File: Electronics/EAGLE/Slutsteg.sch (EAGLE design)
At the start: 152 parts, among them CN1 OSTYK33102030-2, CN2 OSTYK33102030-2, CN3 OSTYK33102030-2, IC1 SPX1117M3-L-3-3_TR, IC10 LM324D, IC11 L78M12ABDT-TR, IC3 ESP32-WROVER-IE-4MB, IC4 TM8211, IC6 TPA3244DDWR, IC7 TPA3251D2DDVR, IC8 LM324D, IC9 LM324D, J1 0532610671, J2 JW-PJ-307-4H, J3 B2P-VH_LF__SN_, SW3 PDB181-K420F-103A2

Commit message: started on the smaller components
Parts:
- added IC2: L78M12ABDT-TR, SamacSys_Parts:L78M12ABDT-TR
- added SJ1: (no value), jumper:SJ
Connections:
- new net VDD2: C47.+, C52.1, IC2.OUTPUT, IC7.VDD, R23.1, R24.1, SJ1.2
- net GND: now also IC2.GND_(THERMALPAD)
- net PVDD: now also IC2.INPUT
- net VDD: now also SJ1.1; no longer C47.+, C52.1, IC7.VDD, R23.1, R24.1
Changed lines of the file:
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@@
 <part name="GND6" library="supply1" library_urn="urn:adsk.eagle:library:371" deviceset="GND" device=""/>
 <part name="GND8" library="supply1" library_urn="urn:adsk.eagle:library:371" deviceset="GND" device=""/>
-<part name="VDD1" library="supply1" library_urn="urn:adsk.eagle:library:371" deviceset="VDD" device=""/>
 <part name="R25" library="rcl" library_urn="urn:adsk.eagle:library:334" deviceset="R-EU_" device="R0603" package3d_urn="urn:adsk.eagle:package:23555/3" value="20K/5%/0.1W"/>
 <part name="FRAME4" library="frames" library_urn="urn:adsk.eagle:library:229" deviceset="A3L-LOC" device=""/>
@@
 <part name="J3" library="SamacSys_Parts" deviceset="B2P-VH_LF__SN_" device="" override_package3d_urn="urn:adsk.eagle:package:27321884/2" override_package_urn="urn:adsk.eagle:footprint:27321885/1"/>
 <part name="GND11" library="supply1" library_urn="urn:adsk.eagle:library:371" deviceset="GND" device=""/>
+<part name="IC2" library="SamacSys_Parts" deviceset="L78M12ABDT-TR" device="" override_package3d_urn="urn:adsk.eagle:package:27319245/2" override_package_urn="urn:adsk.eagle:footprint:27319266/1"/>
+<part name="GND12" library="supply1" library_urn="urn:adsk.eagle:library:371" deviceset="GND" device=""/>
+<part name="SJ1" library="jumper" library_urn="urn:adsk.eagle:library:252" deviceset="SJ" device="" package3d_urn="urn:adsk.eagle:package:15471/1"/>
+<part name="VDD1" library="supply1" library_urn="urn:adsk.eagle:library:371" deviceset="VDD" device=""/>
 </parts>
 <sheets>
@@
 <attribute name="VALUE" x="35.56" y="149.86" size="1.778" layer="96" rot="MR0"/>
 </instance>
+<instance part="IC2" gate="G$1" x="116.84" y="124.46" smashed="yes" rot="MR0">
+<attribute name="NAME" x="92.71" y="132.08" size="1.778" layer="95" align="center-left"/>
+<attribute name="VALUE" x="92.71" y="129.54" size="1.778" layer="96" align="center-left"/>
+</instance>
+<instance part="GND12" gate="1" x="68.58" y="111.76" smashed="yes" rot="MR0">
+<attribute name="VALUE" x="71.12" y="109.22" size="1.778" layer="96" rot="MR0"/>
+</instance>
+<instance part="SJ1" gate="1" x="149.86" y="121.92" smashed="yes" rot="R180">
+<attribute name="NAME" x="152.4" y="119.38" size="1.778" layer="95" rot="R180"/>
+<attribute name="VALUE" x="152.4" y="125.73" size="1.778" layer="96" rot="R180"/>
+</instance>
+<instance part="VDD1" gate="G$1" x="165.1" y="139.7" smashed="yes" rot="MR0">
+<attribute name="VALUE" x="167.64" y="142.24" size="1.778" layer="96" rot="MR180"/>
+</instance>
 </instances>
 <busses>
@@
 <wire x1="33.02" y1="190.5" x2="33.02" y2="154.94" width="0.1524" layer="91"/>
 </segment>
+<segment>
+<pinref part="IC2" gate="G$1" pin="GND_(THERMALPAD)"/>
+<pinref part="GND12" gate="1" pin="GND"/>
+<wire x1="71.12" y1="124.46" x2="68.58" y2="124.46" width="0.1524" layer="91"/>
+<wire x1="68.58" y1="124.46" x2="68.58" y2="114.3" width="0.1524" layer="91"/>
+</segment>
 </net>
 <net name="SPEAKER_L_0" class="0">
@@
 <wire x1="33.02" y1="193.04" x2="33.02" y2="228.6" width="0.1524" layer="91"/>
 <label x="33.02" y="228.6" size="1.778" layer="95" xref="yes"/>
+</segment>
+<segment>
+<pinref part="IC2" gate="G$1" pin="INPUT"/>
+<wire x1="116.84" y1="124.46" x2="121.92" y2="124.46" width="0.1524" layer="91"/>
+<wire x1="121.92" y1="124.46" x2="121.92" y2="142.24" width="0.1524" layer="91"/>
+<label x="121.92" y="142.24" size="1.778" layer="95" xref="yes"/>
 </segment>
 </net>
@@
 <wire x1="144.78" y1="175.26" x2="144.78" y2="190.5" width="0.1524" layer="91"/>
 <junction x="144.78" y="190.5"/>
+</segment>
+<segment>
+<pinref part="SJ1" gate="1" pin="1"/>
+<wire x1="154.94" y1="121.92" x2="165.1" y2="121.92" width="0.1524" layer="91"/>
+<pinref part="VDD1" gate="G$1" pin="VDD"/>
+<wire x1="165.1" y1="121.92" x2="165.1" y2="137.16" width="0.1524" layer="91"/>
 </segment>
 </net>
@@
 <wire x1="337.82" y1="160.02" x2="332.74" y2="160.02" width="0.1524" layer="91"/>
 <label x="332.74" y="160.02" size="1.778" layer="95" rot="R180" xref="yes"/>
+</segment>
+</net>
+<net name="VDD2" class="0">
+<segment>
+<pinref part="IC2" gate="G$1" pin="OUTPUT"/>
+<wire x1="116.84" y1="121.92" x2="139.7" y2="121.92" width="0.1524" layer="91"/>
+<wire x1="139.7" y1="121.92" x2="139.7" y2="129.54" width="0.1524" layer="91"/>
+<label x="139.7" y="129.54" size="1.778" layer="95" xref="yes"/>
+<pinref part="SJ1" gate="1" pin="2"/>
+<wire x1="144.78" y1="121.92" x2="139.7" y2="121.92" width="0.1524" layer="91"/>
+<junction x="139.7" y="121.92"/>
 </segment>
 </net>
@@
 <instance part="GND8" gate="1" x="127" y="162.56" smashed="yes">
 <attribute name="VALUE" x="124.46" y="160.02" size="1.778" layer="96"/>
-</instance>
-<instance part="VDD1" gate="G$1" x="99.06" y="205.74" smashed="yes">
-<attribute name="VALUE" x="99.06" y="208.28" size="1.778" layer="96"/>
 </instance>
 <instance part="R25" gate="G$1" x="139.7" y="149.86" smashed="yes">
@@
 </segment>
 </net>
-<net name="VDD" class="0">
-<segment>
-<wire x1="121.92" y1="111.76" x2="99.06" y2="111.76" width="0.1524" layer="91"/>
-<wire x1="99.06" y1="111.76" x2="99.06" y2="185.42" width="0.1524" layer="91"/>
-<wire x1="99.06" y1="185.42" x2="99.06" y2="203.2" width="0.1524" layer="91"/>
-<junction x="99.06" y="185.42"/>
-<pinref part="IC7" gate="G$1" pin="VDD"/>
-<wire x1="139.7" y1="162.56" x2="147.32" y2="162.56" width="0.1524" layer="91"/>
-<wire x1="139.7" y1="185.42" x2="139.7" y2="162.56" width="0.1524" layer="91"/>
-<pinref part="R24" gate="G$1" pin="1"/>
-<pinref part="VDD1" gate="G$1" pin="VDD"/>
-<wire x1="99.06" y1="185.42" x2="114.3" y2="185.42" width="0.1524" layer="91"/>
-<wire x1="114.3" y1="185.42" x2="127" y2="185.42" width="0.1524" layer="91"/>
-<wire x1="127" y1="185.42" x2="139.7" y2="185.42" width="0.1524" layer="91"/>
-<junction x="114.3" y="185.42"/>
-<wire x1="127" y1="180.34" x2="127" y2="185.42" width="0.1524" layer="91"/>
-<junction x="127" y="185.42"/>
-<pinref part="R23" gate="G$1" pin="1"/>
-<wire x1="114.3" y1="187.96" x2="121.92" y2="187.96" width="0.1524" layer="91"/>
-<wire x1="114.3" y1="185.42" x2="114.3" y2="187.96" width="0.1524" layer="91"/>
-<pinref part="C47" gate="G$1" pin="+"/>
-<wire x1="114.3" y1="182.88" x2="114.3" y2="185.42" width="0.1524" layer="91"/>
-<pinref part="C52" gate="G$1" pin="1"/>
-</segment>
-</net>
 <net name="N$36" class="0">
 <segment>
@@
 </segment>
 </net>
+<net name="VDD2" class="0">
+<segment>
+<wire x1="121.92" y1="111.76" x2="99.06" y2="111.76" width="0.1524" layer="91"/>
+<wire x1="99.06" y1="111.76" x2="99.06" y2="185.42" width="0.1524" layer="91"/>
+<wire x1="99.06" y1="185.42" x2="99.06" y2="203.2" width="0.1524" layer="91"/>
+<junction x="99.06" y="185.42"/>
+<pinref part="IC7" gate="G$1" pin="VDD"/>
+<wire x1="139.7" y1="162.56" x2="147.32" y2="162.56" width="0.1524" layer="91"/>
+<wire x1="139.7" y1="185.42" x2="139.7" y2="162.56" width="0.1524" layer="91"/>
+<pinref part="R24" gate="G$1" pin="1"/>
+<wire x1="99.06" y1="185.42" x2="114.3" y2="185.42" width="0.1524" layer="91"/>
+<wire x1="114.3" y1="185.42" x2="127" y2="185.42" width="0.1524" layer="91"/>
+<wire x1="127" y1="185.42" x2="139.7" y2="185.42" width="0.1524" layer="91"/>
+<junction x="114.3" y="185.42"/>
+<wire x1="127" y1="180.34" x2="127" y2="185.42" width="0.1524" layer="91"/>
+<junction x="127" y="185.42"/>
+<pinref part="R23" gate="G$1" pin="1"/>
+<wire x1="114.3" y1="187.96" x2="121.92" y2="187.96" width="0.1524" layer="91"/>
+<wire x1="114.3" y1="185.42" x2="114.3" y2="187.96" width="0.1524" layer="91"/>
+<pinref part="C47" gate="G$1" pin="+"/>
+<wire x1="114.3" y1="182.88" x2="114.3" y2="185.42" width="0.1524" layer="91"/>
+<pinref part="C52" gate="G$1" pin="1"/>
+<label x="99.06" y="203.2" size="1.778" layer="95" xref="yes"/>
+</segment>
+</net>

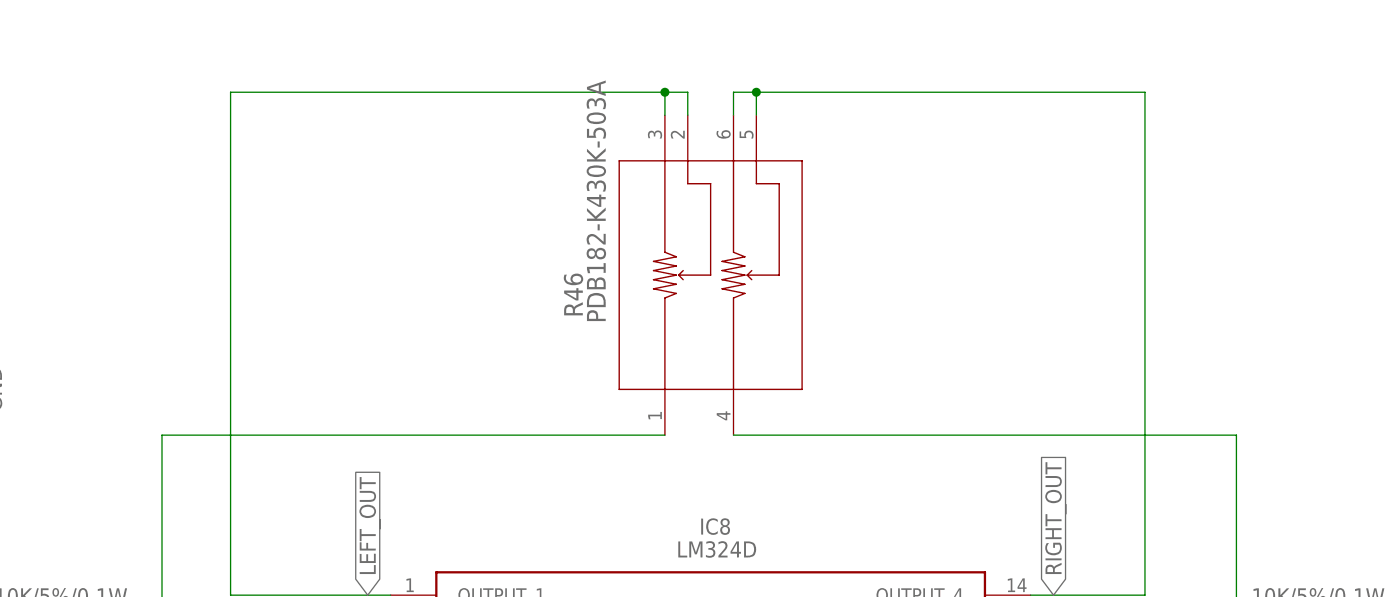
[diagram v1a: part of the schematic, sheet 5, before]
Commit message: PCB-layout: dragit till första opampstegen
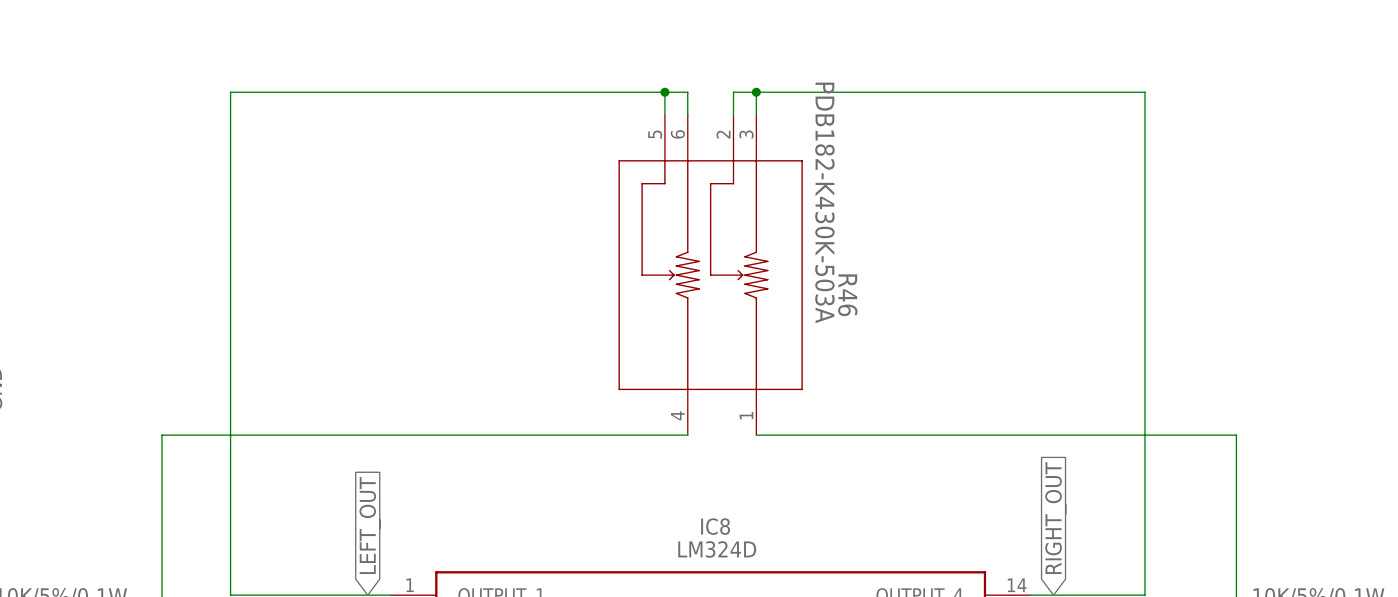
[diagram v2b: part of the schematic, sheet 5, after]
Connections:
- net LEFT_OUT: now also R46.5, R46.6; no longer R46.2, R46.3
- net N$71: now also R46.4; no longer R46.1
- net N$74: now also R46.1; no longer R46.4
- net RIGHT_OUT: now also R46.2, R46.3; no longer R46.5, R46.6
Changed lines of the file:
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@@
 <attribute name="VALUE" x="136.144" y="46.101" size="1.778" layer="96"/>
 </instance>
-<instance part="R46" gate="A" x="187.96" y="208.28" smashed="yes" rot="R90">
-<attribute name="NAME" x="178.8414" y="223.8756" size="2.0828" layer="95" ratio="6" rot="SR90"/>
-<attribute name="VALUE" x="181.3814" y="223.2406" size="2.0828" layer="96" ratio="6" rot="SR90"/>
+<instance part="R46" gate="A" x="198.12" y="208.28" smashed="yes" rot="MR90">
+<attribute name="NAME" x="207.2386" y="223.8756" size="2.0828" layer="95" ratio="6" rot="SMR90"/>
+<attribute name="VALUE" x="204.6986" y="223.2406" size="2.0828" layer="96" ratio="6" rot="SMR90"/>
 </instance>
 </instances>
@@
 <pinref part="R35" gate="G$1" pin="1"/>
 <wire x1="157.48" y1="190.5" x2="132.08" y2="190.5" width="0.1524" layer="91"/>
-<pinref part="R46" gate="A" pin="1"/>
 <wire x1="132.08" y1="190.5" x2="127" y2="190.5" width="0.1524" layer="91"/>
 <wire x1="132.08" y1="190.5" x2="132.08" y2="210.82" width="0.1524" layer="91"/>
-<wire x1="132.08" y1="210.82" x2="187.96" y2="210.82" width="0.1524" layer="91"/>
 <junction x="132.08" y="190.5"/>
+<pinref part="R46" gate="A" pin="4"/>
+<wire x1="190.5" y1="210.82" x2="132.08" y2="210.82" width="0.1524" layer="91"/>
 </segment>
 </net>
@@
 <wire x1="139.7" y1="193.04" x2="157.48" y2="193.04" width="0.1524" layer="91"/>
 <label x="154.94" y="193.04" size="1.778" layer="95" rot="R90" xref="yes"/>
-<pinref part="R46" gate="A" pin="2"/>
-<wire x1="190.5" y1="246.38" x2="190.5" y2="248.92" width="0.1524" layer="91"/>
-<wire x1="190.5" y1="248.92" x2="187.96" y2="248.92" width="0.1524" layer="91"/>
-<pinref part="R46" gate="A" pin="3"/>
-<wire x1="187.96" y1="248.92" x2="187.96" y2="246.38" width="0.1524" layer="91"/>
 <wire x1="139.7" y1="193.04" x2="139.7" y2="248.92" width="0.1524" layer="91"/>
 <wire x1="139.7" y1="248.92" x2="187.96" y2="248.92" width="0.1524" layer="91"/>
+<pinref part="R46" gate="A" pin="6"/>
+<wire x1="187.96" y1="248.92" x2="190.5" y2="248.92" width="0.1524" layer="91"/>
+<wire x1="190.5" y1="246.38" x2="190.5" y2="248.92" width="0.1524" layer="91"/>
+<pinref part="R46" gate="A" pin="5"/>
+<wire x1="187.96" y1="246.38" x2="187.96" y2="248.92" width="0.1524" layer="91"/>
 <junction x="187.96" y="248.92"/>
 </segment>
@@
 <junction x="251.46" y="190.5"/>
 <wire x1="251.46" y1="190.5" x2="251.46" y2="210.82" width="0.1524" layer="91"/>
-<pinref part="R46" gate="A" pin="4"/>
-<wire x1="251.46" y1="210.82" x2="195.58" y2="210.82" width="0.1524" layer="91"/>
+<pinref part="R46" gate="A" pin="1"/>
+<wire x1="198.12" y1="210.82" x2="251.46" y2="210.82" width="0.1524" layer="91"/>
 </segment>
 </net>
@@
 <wire x1="241.3" y1="193.04" x2="241.3" y2="248.92" width="0.1524" layer="91"/>
 <label x="231.14" y="193.04" size="1.778" layer="95" rot="R90" xref="yes"/>
-<pinref part="R46" gate="A" pin="6"/>
+<wire x1="241.3" y1="248.92" x2="198.12" y2="248.92" width="0.1524" layer="91"/>
+<pinref part="R46" gate="A" pin="2"/>
+<wire x1="198.12" y1="248.92" x2="195.58" y2="248.92" width="0.1524" layer="91"/>
 <wire x1="195.58" y1="246.38" x2="195.58" y2="248.92" width="0.1524" layer="91"/>
-<pinref part="R46" gate="A" pin="5"/>
-<wire x1="195.58" y1="248.92" x2="198.12" y2="248.92" width="0.1524" layer="91"/>
-<wire x1="198.12" y1="248.92" x2="198.12" y2="246.38" width="0.1524" layer="91"/>
-<wire x1="241.3" y1="248.92" x2="198.12" y2="248.92" width="0.1524" layer="91"/>
+<pinref part="R46" gate="A" pin="3"/>
+<wire x1="198.12" y1="246.38" x2="198.12" y2="248.92" width="0.1524" layer="91"/>
 <junction x="198.12" y="248.92"/>
 </segment>

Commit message: Connected more things in the layout.  Added a heatsink and lib file for it.
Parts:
- removed C24, C82: 10uF/16V, rcl:C-EUC0805
- removed J3: B2P-VH_LF__SN_, SamacSys_Parts:B2P-VH_LF__SN_
- added J4: B4P-VH_LF__SN_, B4P-VH_LF__SN_:B4P-VH_LF__SN_
- added U$1, U$2: V5618C, V5618C:V5618C
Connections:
- removed net INPUT_B: C24.1
- removed net INPUT_D: C82.1
- removed net N$61: C82.2, IC6.INPUT_D
- removed net N$63: C24.2, IC6.INPUT_B
- new net N$5: IC10.INVERTING_INPUT_3, IC10.OUTPUT_3
- net 6V_BUFFER: now also IC10.NON-INVERTING_INPUT_3
- net GND: now also IC6.INPUT_B, IC6.INPUT_D, J4.2, J4.3; no longer J3.1
- net PVDD: now also J4.1, J4.4; no longer J3.2
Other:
- moved on the sheet: C1, C10, C11, C12, C13, C14, C2, C3, C6, C7, C8, C9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

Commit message: PANIC, lagt till extra OP
Kör DIFF input på alla klass D
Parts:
- added C24, C76: 1uF/50V, rcl:C-EUC0805
- added C82, C83: 10uF/16V, rcl:C-EUC0805
- added IC5: LM324D, SamacSys_Parts:LM324D
- added R47, R48, R51, R52, R53, R54: 100K/5%/0.1W, rcl:R-EU_R0603
- added R49, R50: 10K/5%/0.1W, rcl:R-EU_R0603
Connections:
- new net 6V_BUFFER2: IC5.INVERTING_INPUT_2, IC5.NON-INVERTING_INPUT_1, IC5.NON-INVERTING_INPUT_3, IC5.NON-INVERTING_INPUT_4, IC5.OUTPUT_2
- new net BASE_OUT2: IC5.OUTPUT_1, R50.1
- new net INPUT_B: C83.1
- new net INPUT_D: C82.1
- new net LEFT_OUT2: IC5.OUTPUT_4, R51.2
- new net N$10: C83.2, IC6.INPUT_B
- new net N$12: IC5.INVERTING_INPUT_3, R53.1, R54.2
- new net N$6: C24.1, IC5.NON-INVERTING_INPUT_2, R47.1, R48.2
- new net N$7: C82.2, IC6.INPUT_D
- new net N$8: IC5.INVERTING_INPUT_4, R51.1, R52.2
- new net N$9: IC5.INVERTING_INPUT_1, R49.1, R50.2
- new net RIGHT_OUT2: IC5.OUTPUT_3, R53.2
- net BASE_OUT: now also R49.2
- net GND: now also C24.2, C76.2, IC5.VCC-, R48.1; no longer IC6.INPUT_B, IC6.INPUT_D
- net LEFT_OUT: now also R52.1
- net RIGHT_OUT: now also R54.1
- net VDD: now also C76.1, IC5.VCC+, R47.2

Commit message: Cleaned up TPA3251
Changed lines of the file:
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@@
 <instance part="C60" gate="G$1" x="208.28" y="116.84" smashed="yes">
 <attribute name="NAME" x="209.804" y="117.221" size="1.778" layer="95"/>
-<attribute name="VALUE" x="209.804" y="112.141" size="1.778" layer="96"/>
+<attribute name="VALUE" x="204.724" y="112.141" size="1.778" layer="96"/>
 </instance>
 <instance part="C56" gate="G$1" x="198.12" y="116.84" smashed="yes">
 <attribute name="NAME" x="199.644" y="117.221" size="1.778" layer="95"/>
-<attribute name="VALUE" x="199.644" y="112.141" size="1.778" layer="96"/>
+<attribute name="VALUE" x="194.564" y="112.141" size="1.778" layer="96"/>
 </instance>
 <instance part="C57" gate="G$1" x="200.66" y="157.48" smashed="yes">
 <attribute name="NAME" x="202.184" y="157.861" size="1.778" layer="95"/>
-<attribute name="VALUE" x="202.184" y="152.781" size="1.778" layer="96"/>
+<attribute name="VALUE" x="197.104" y="152.781" size="1.778" layer="96"/>
 </instance>
 <instance part="C59" gate="G$1" x="208.28" y="157.48" smashed="yes">
 <attribute name="NAME" x="209.804" y="157.861" size="1.778" layer="95"/>
-<attribute name="VALUE" x="209.804" y="152.781" size="1.778" layer="96"/>
+<attribute name="VALUE" x="207.264" y="152.781" size="1.778" layer="96"/>
 </instance>
 <instance part="C52" gate="G$1" x="127" y="177.8" smashed="yes">
